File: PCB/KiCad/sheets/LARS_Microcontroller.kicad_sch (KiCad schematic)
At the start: 30 parts, among them J1 Reset Header, J2 SWD Flash, SW1 Reset, U1 STM32F429ZIT6TR, Y1 IQXO-791 8.00MHz

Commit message: add final traces
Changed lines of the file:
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@@
 	(wire
 		(pts
-			(xy 132.08 40.64) (xy 142.24 40.64)
+			(xy 132.08 41.91) (xy 140.97 41.91)
 		)
 		(stroke
@@
 	(wire
 		(pts
+			(xy 140.97 40.64) (xy 142.24 40.64)
+		)
+		(stroke
+			(width 0)
+			(type default)
+		)
+	)
+	(wire
+		(pts
 			(xy 57.15 177.8) (xy 57.15 179.07)
 		)
@@
 	(wire
 		(pts
-			(xy 68.58 52.07) (xy 78.74 52.07)
+			(xy 68.58 52.07) (xy 72.39 52.07)
 		)
 		(stroke
@@
 	(wire
 		(pts
-			(xy 132.08 38.1) (xy 142.24 38.1)
+			(xy 140.97 38.1) (xy 142.24 38.1)
 		)
 		(stroke
@@
 	(wire
 		(pts
+			(xy 140.97 41.91) (xy 140.97 40.64)
+		)
+		(stroke
+			(width 0)
+			(type default)
+		)
+	)
+	(wire
+		(pts
 			(xy 69.85 179.07) (xy 69.85 177.8)
 		)
@@
 	)
 	(label "STM_BOOT0"
-		(at 132.08 40.64 0)
+		(at 132.08 41.91 0)
 		(effects
 			(font
@@
 	(label "RESET"
 		(at 39.37 52.07 0)
-		(effects
-			(font
-				(size 1.016 1.016)
-			)
-			(justify left bottom)
-		)
-	)
-	(label "STM_NRST"
-		(at 78.74 52.07 180)
-		(effects
-			(font
-				(size 1.016 1.016)
-			)
-			(justify right bottom)
-		)
-	)
-	(label "STM_NRST"
-		(at 132.08 38.1 0)
 		(effects
 			(font
@@
 			(effects
 				(font
+					(size 1.27 1.27)
+				)
+				(justify left)
+				(hide yes)
+			)
+		)
+	)
+	(global_label "STM_NRST"
+		(shape input)
+		(at 140.97 38.1 180)
+		(fields_autoplaced yes)
+		(effects
+			(font
+				(size 1.016 1.016)
+			)
+			(justify right)
+		)
+		(property "Intersheetrefs" "${INTERSHEET_REFS}"
+			(at 131.0831 38.1 0)
+			(effects
+				(font
+					(size 1.27 1.27)
+				)
+				(justify right)
+				(hide yes)
+			)
+		)
+	)
+	(global_label "STM_NRST"
+		(shape output)
+		(at 72.39 52.07 0)
+		(fields_autoplaced yes)
+		(effects
+			(font
+				(size 1.016 1.016)
+			)
+			(justify left)
+		)
+		(property "Intersheetrefs" "${INTERSHEET_REFS}"
+			(at 82.2769 52.07 0)
+			(effects
+				(font

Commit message: finish PCB routing
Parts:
- C2: value 1u -> 2u2
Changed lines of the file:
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@@
 			)
 		)
-		(property "Value" "1u"
+		(property "Value" "2u2"
 			(at 93.218 118.872 0)
 			(effects

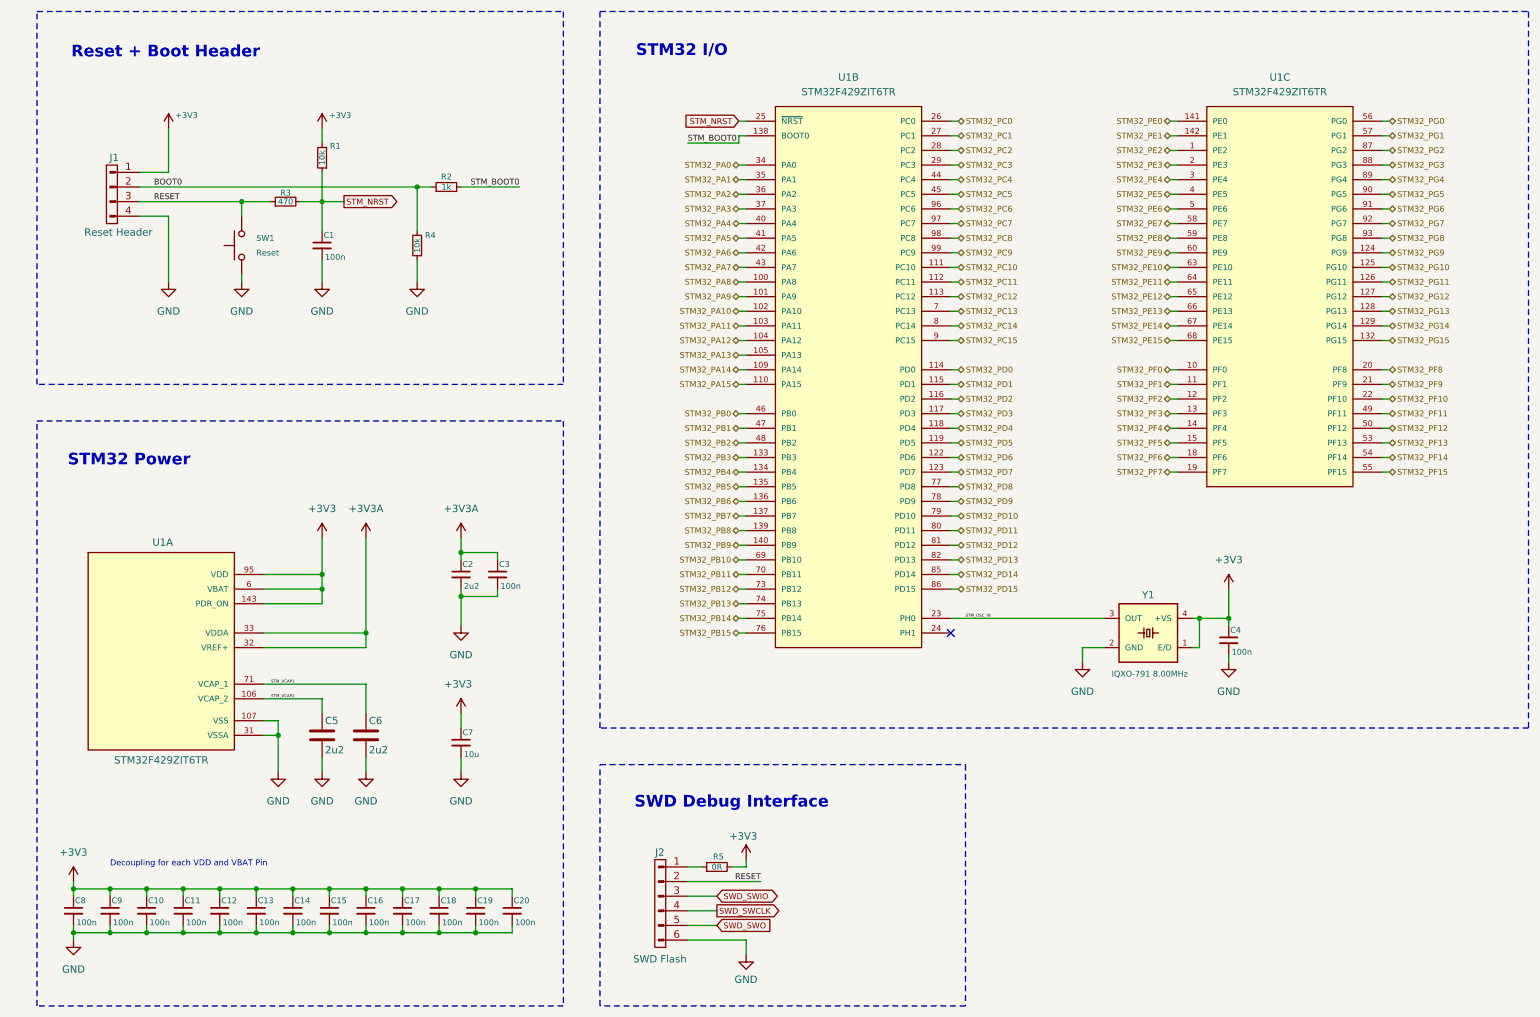
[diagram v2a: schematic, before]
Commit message: change default KiCad schematic font
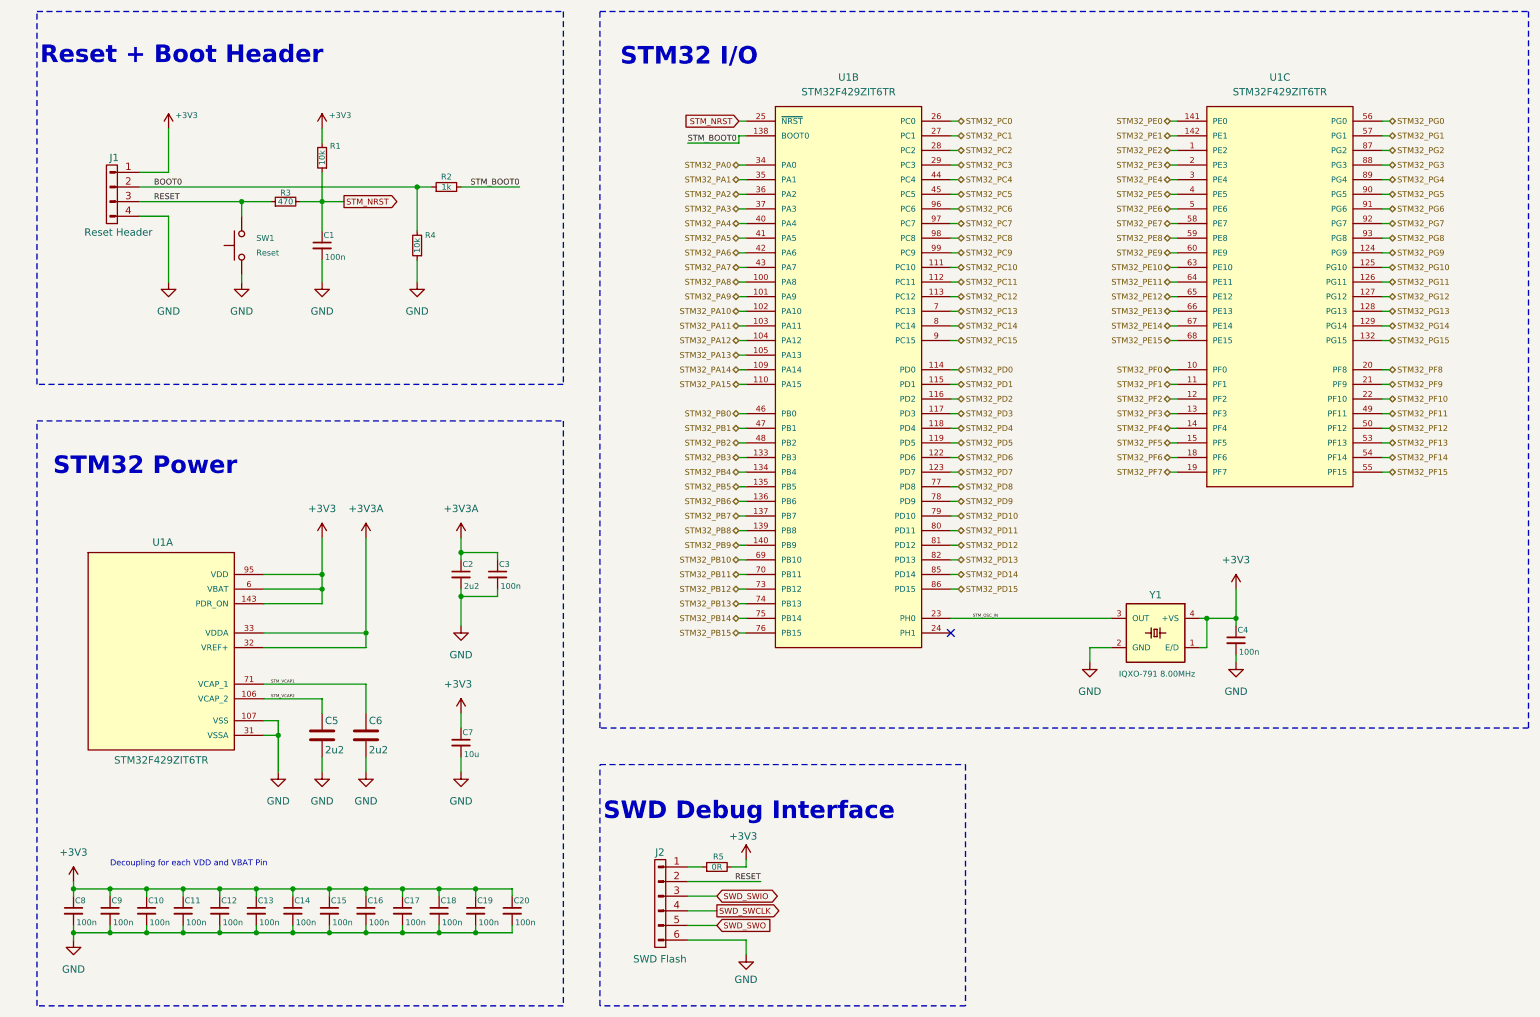
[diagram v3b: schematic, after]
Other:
- moved on the sheet: C4, Y1
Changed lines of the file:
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@@
 	(text "Reset + Boot Header"
 		(exclude_from_sim no)
-		(at 41.402 26.162 0)
+		(at 44.196 26.67 0)
 		(effects
 			(font
-				(size 2.032 2.032)
+				(size 3.048 3.048)
 				(thickness 0.4064)
 				(bold yes)
@@
 	(text "SWD Debug Interface"
 		(exclude_from_sim no)
-		(at 139.7 156.464 0)
+		(at 142.748 157.988 0)
 		(effects
 			(font
-				(size 2.032 2.032)
+				(size 3.048 3.048)
 				(thickness 0.4064)
 				(bold yes)
@@
 	(text "STM32 I/O"
 		(exclude_from_sim no)
-		(at 131.064 25.908 0)
+		(at 132.334 26.924 0)
 		(effects
 			(font
-				(size 2.032 2.032)
+				(size 3.048 3.048)
 				(thickness 0.4064)
 				(bold yes)
@@
 	(text "STM32 Power"
 		(exclude_from_sim no)
-		(at 35.052 97.028 0)
+		(at 37.846 98.044 0)
 		(effects
 			(font
-				(size 2.032 2.032)
+				(size 3.048 3.048)
 				(thickness 0.4064)
 				(bold yes)
@@
 	)
 	(junction
-		(at 220.98 124.46)
+		(at 222.25 124.46)
 		(diameter 0)
 		(color 0 0 0 0)
@@
 	)
 	(junction
-		(at 226.06 124.46)
+		(at 227.33 124.46)
 		(diameter 0)
 		(color 0 0 0 0)
@@
 	(wire
 		(pts
-			(xy 200.66 129.54) (xy 204.47 129.54)
+			(xy 201.93 129.54) (xy 205.74 129.54)
 		)
 		(stroke
@@
 	(wire
 		(pts
-			(xy 219.71 124.46) (xy 220.98 124.46)
+			(xy 220.98 124.46) (xy 222.25 124.46)
 		)
 		(stroke
@@
 	(wire
 		(pts
-			(xy 226.06 132.08) (xy 226.06 130.81)
+			(xy 227.33 132.08) (xy 227.33 130.81)
 		)
 		(stroke
@@
 	(wire
 		(pts
-			(xy 220.98 129.54) (xy 219.71 129.54)
+			(xy 222.25 129.54) (xy 220.98 129.54)
 		)
 		(stroke
@@
 	(wire
 		(pts
-			(xy 220.98 124.46) (xy 226.06 124.46)
+			(xy 222.25 124.46) (xy 227.33 124.46)
 		)
 		(stroke
@@
 	(wire
 		(pts
-			(xy 177.8 124.46) (xy 204.47 124.46)
-		)
-		(stroke
-			(width 0)
-			(type default)
-		)
-	)
-	(wire
-		(pts
 			(xy 179.07 101.6) (xy 177.8 101.6)
 		)
@@
 	(wire
 		(pts
-			(xy 200.66 129.54) (xy 200.66 132.08)
+			(xy 201.93 129.54) (xy 201.93 132.08)
 		)
 		(stroke
@@
 	(wire
 		(pts
-			(xy 226.06 125.73) (xy 226.06 124.46)
+			(xy 227.33 125.73) (xy 227.33 124.46)
 		)
 		(stroke
@@
 	(wire
 		(pts
-			(xy 226.06 119.38) (xy 226.06 124.46)
+			(xy 227.33 119.38) (xy 227.33 124.46)
 		)
 		(stroke
@@
 	(wire
 		(pts
+			(xy 177.8 124.46) (xy 205.74 124.46)
+		)
+		(stroke
+			(width 0)
+			(type default)
+		)
+	)
+	(wire
+		(pts
 			(xy 44.45 171.45) (xy 50.8 171.45)
 		)
@@
 	(wire
 		(pts
-			(xy 220.98 124.46) (xy 220.98 129.54)
+			(xy 222.25 124.46) (xy 222.25 129.54)
 		)
 		(stroke
@@
 	)
 	(label "STM_OSC_IN"
-		(at 180.34 124.46 0)
+		(at 181.61 124.46 0)
 		(effects
 			(font
@@
 	(symbol
 		(lib_id "power:+3.3V")
-		(at 226.06 119.38 0)
+		(at 227.33 119.38 0)
 		(unit 1)
 		(exclude_from_sim no)
@@
 		(fields_autoplaced yes)
 		(property "Reference" "#PWR010"
-			(at 226.06 123.19 0)
+			(at 227.33 123.19 0)
 			(effects
 				(font
@@
 		)
 		(property "Value" "+3V3"
-			(at 226.06 114.3 0)
+			(at 227.33 114.3 0)
 			(effects
 				(font
@@
 		)
 		(property "Footprint" ""
-			(at 226.06 119.38 0)
+			(at 227.33 119.38 0)
 			(effects
 				(font
@@
 		)
 		(property "Datasheet" ""
-			(at 226.06 119.38 0)
+			(at 227.33 119.38 0)
 			(effects
 				(font
@@
 		)
 		(property "Description" "Power symbol creates a global label with name \"+3.3V\""
-			(at 226.06 119.38 0)
+			(at 227.33 119.38 0)
 			(effects
 				(font
@@
 	(symbol
 		(lib_id "LARS_Hardware_Interface:WE-SPXO_IQXO-791")
-		(at 212.09 127 0)
+		(at 213.36 127 0)
 		(mirror y)
 		(unit 1)
@@
 		(dnp no)
 		(property "Reference" "Y1"
-			(at 212.09 120.396 0)
+			(at 213.36 120.396 0)
 			(effects
 				(font
@@
 		)
 		(property "Value" "IQXO-791 8.00MHz"
-			(at 212.344 134.112 0)
+			(at 213.614 134.112 0)
 			(effects
 				(font
@@
 		)
 		(property "Footprint" "LARS_Hardware_Interface:WE-SPXO_IQXO-791"
-			(at 217.17 127 0)
+			(at 218.44 127 0)
 			(effects
 				(font
@@
 		)
 		(property "Datasheet" ""
-			(at 212.09 127 0)
+			(at 213.36 127 0)
 			(effects
 				(font
@@
 		)
 		(property "Description" ""
-			(at 212.09 127 0)
+			(at 213.36 127 0)
 			(effects
 				(font
@@
 		)
 		(property "MF" "Würth Elektronik"
-			(at 212.09 127 0)
+			(at 213.36 127 0)
 			(effects
 				(font
@@
 		)
 		(property "Description_1" "\n                        \n                            WE-SPXO CRYSTAL OSCILLATOR 8.0 M\n                        \n"
-			(at 217.17 127 0)
+			(at 218.44 127 0)
 			(effects
 				(font
@@
 		)
 		(property "Package" "None"
-			(at 212.09 127 0)
+			(at 213.36 127 0)
 			(effects
 				(font
@@
 		)
 		(property "Price" "None"
-			(at 212.09 127 0)
+			(at 213.36 127 0)
 			(effects
 				(font
@@
 		)
 		(property "SnapEDA_Link" "https://www.snapeda.com/parts/831072801/W%25C3%25BCrth+Elektronik+Midcom/view-part/?ref=snap"
-			(at 217.17 127 0)
+			(at 218.44 127 0)
 			(effects
 				(font
@@
 		)
 		(property "MP" "831072801"
-			(at 212.09 127 0)
+			(at 213.36 127 0)
 			(effects
 				(font
@@
 		)
 		(property "Availability" "In Stock"
-			(at 212.09 127 0)
+			(at 213.36 127 0)
 			(effects
 				(font
@@
 		)
 		(property "Check_prices" "https://www.snapeda.com/parts/831072801/W%25C3%25BCrth+Elektronik+Midcom/view-part/?ref=eda"
-			(at 217.17 127 0)
+			(at 218.44 127 0)
 			(effects
 				(font
@@
 	(symbol
 		(lib_id "power:GND")
-		(at 200.66 132.08 0)
+		(at 201.93 132.08 0)
 		(unit 1)
 		(exclude_from_sim no)
@@
 		(fields_autoplaced yes)
 		(property "Reference" "#PWR012"
-			(at 200.66 138.43 0)
+			(at 201.93 138.43 0)
 			(effects
 				(font
@@
 		)
 		(property "Value" "GND"
-			(at 200.66 137.16 0)
+			(at 201.93 137.16 0)
 			(effects
 				(font
@@
 		)
 		(property "Footprint" ""
-			(at 200.66 132.08 0)
+			(at 201.93 132.08 0)
 			(effects
 				(font
@@
 		)
 		(property "Datasheet" ""
-			(at 200.66 132.08 0)
+			(at 201.93 132.08 0)
 			(effects
 				(font
@@
 		)
 		(property "Description" "Power symbol creates a global label with name \"GND\" , ground"
-			(at 200.66 132.08 0)
+			(at 201.93 132.08 0)
 			(effects
 				(font
@@
 	(symbol
 		(lib_id "power:GND")
-		(at 226.06 132.08 0)
+		(at 227.33 132.08 0)
 		(unit 1)
 		(exclude_from_sim no)
@@
 		(fields_autoplaced yes)
 		(property "Reference" "#PWR013"
-			(at 226.06 138.43 0)
+			(at 227.33 138.43 0)
 			(effects
 				(font
@@
 		)
 		(property "Value" "GND"
-			(at 226.06 137.16 0)
+			(at 227.33 137.16 0)
 			(effects
 				(font
@@
 		)
 		(property "Footprint" ""
-			(at 226.06 132.08 0)
+			(at 227.33 132.08 0)
 			(effects
 				(font
@@
 		)
 		(property "Datasheet" ""
-			(at 226.06 132.08 0)
+			(at 227.33 132.08 0)
 			(effects
 				(font
@@
 		)
 		(property "Description" "Power symbol creates a global label with name \"GND\" , ground"
-			(at 226.06 132.08 0)
+			(at 227.33 132.08 0)
 			(effects
 				(font
@@
 	(symbol
 		(lib_id "LARS_Hardware_Interface:C_Small")
-		(at 226.06 128.27 0)
+		(at 227.33 128.27 0)
 		(unit 1)
 		(exclude_from_sim no)
@@
 		(dnp no)
 		(property "Reference" "C4"
-			(at 226.314 126.492 0)
+			(at 227.584 126.492 0)
 			(effects
 				(font
@@
 		)
 		(property "Value" "100n"
-			(at 226.568 130.302 0)
+			(at 227.838 130.302 0)
 			(effects
 				(font
@@
 		)
 		(property "Footprint" "LARS_Hardware_Interface:C_0805_2012Metric"
-			(at 226.06 128.27 0)
+			(at 227.33 128.27 0)
 			(effects
 				(font
@@
 		)
 		(property "Datasheet" "~"
-			(at 226.06 128.27 0)
+			(at 227.33 128.27 0)
 			(effects
 				(font
@@
 		)
 		(property "Description" "Unpolarized capacitor, small symbol"
-			(at 226.06 128.27 0)
+			(at 227.33 128.27 0)
 			(effects
 				(font

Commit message: update text layout and fix remaining DRC errors
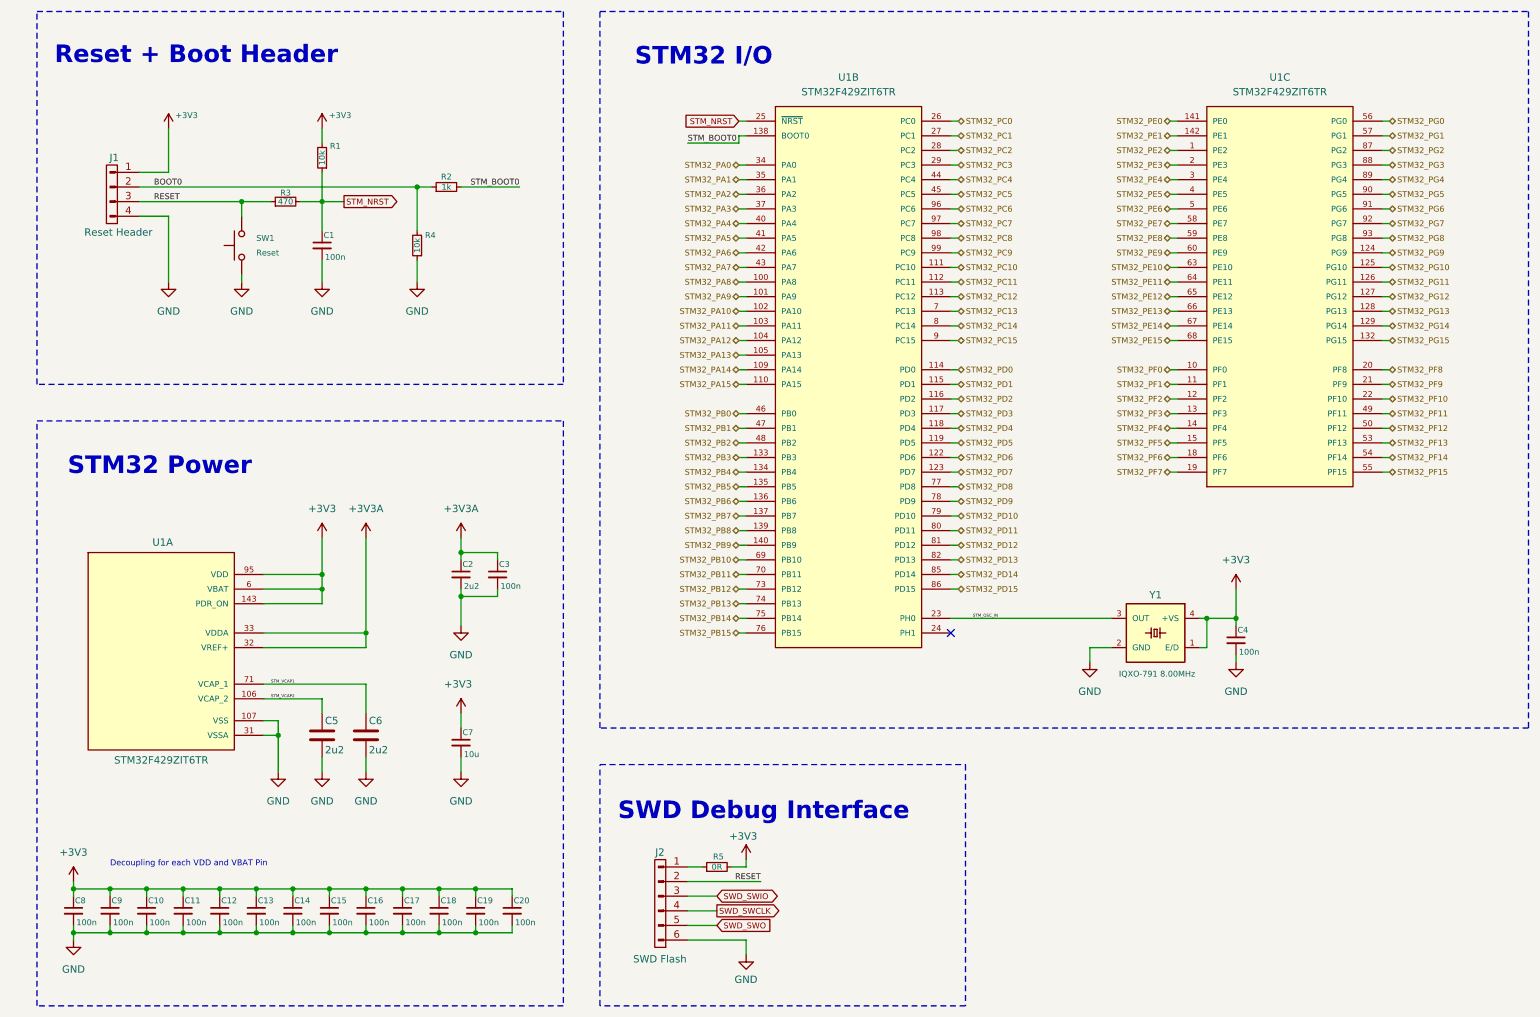
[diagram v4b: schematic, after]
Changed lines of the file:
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@@
 	(text "Reset + Boot Header"
 		(exclude_from_sim no)
-		(at 44.196 26.67 0)
+		(at 46.736 26.67 0)
 		(effects
 			(font
@@
 	(text "SWD Debug Interface"
 		(exclude_from_sim no)
-		(at 142.748 157.988 0)
+		(at 145.288 157.988 0)
 		(effects
 			(font
@@
 	(text "STM32 I/O"
 		(exclude_from_sim no)
-		(at 132.334 26.924 0)
+		(at 134.874 26.924 0)
 		(effects
 			(font
@@
 	(text "STM32 Power"
 		(exclude_from_sim no)
-		(at 37.846 98.044 0)
+		(at 40.386 98.044 0)
 		(effects
 			(font

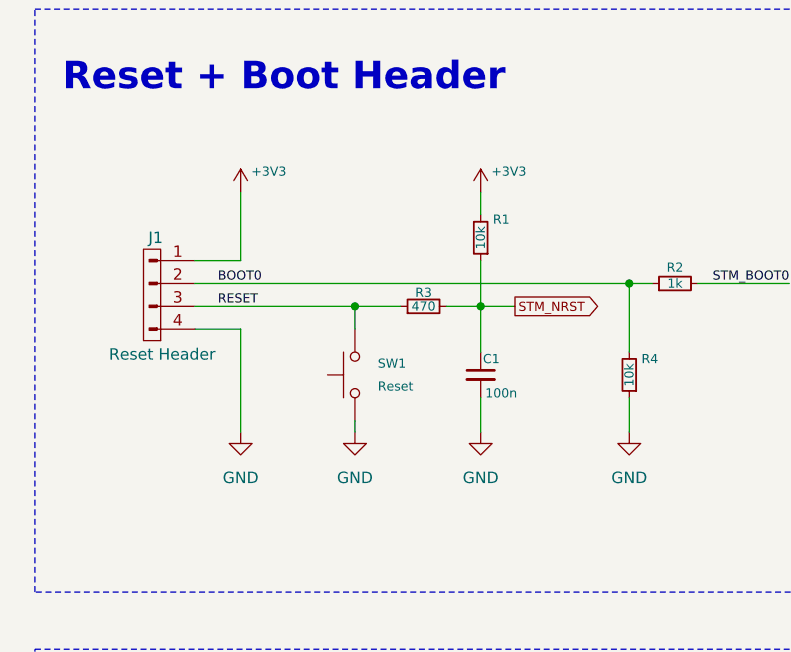
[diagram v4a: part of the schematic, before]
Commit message: add ESD protection and update footprints
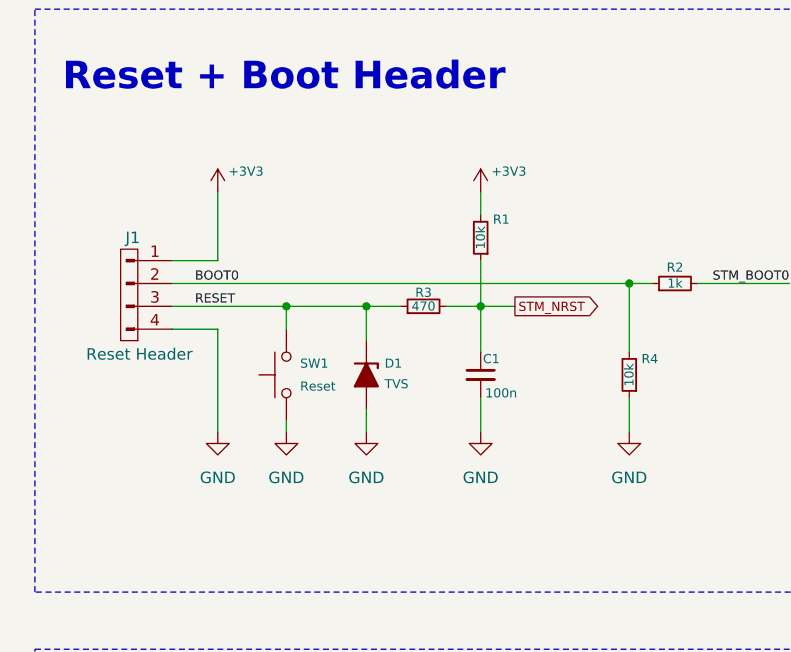
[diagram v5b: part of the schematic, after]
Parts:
- added D1: TVS, LARS_Hardware_Interface:STS321050U182, symbol LARS_Hardware_Interface:D_TVS
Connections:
- net GND: now also D1.2 (A)
- net RESET: now also D1.1 (K)
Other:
- moved on the sheet: J1, SW1
